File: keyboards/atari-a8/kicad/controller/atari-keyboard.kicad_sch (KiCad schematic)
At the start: 31 parts, among them J101 PLAYER 1, J102 5V, J103 I2C DISPLAY, SW101 RESET, U101 Elite-C, U102 MAX7219, U103 MAX7219, U104 7402, U105 74LS08

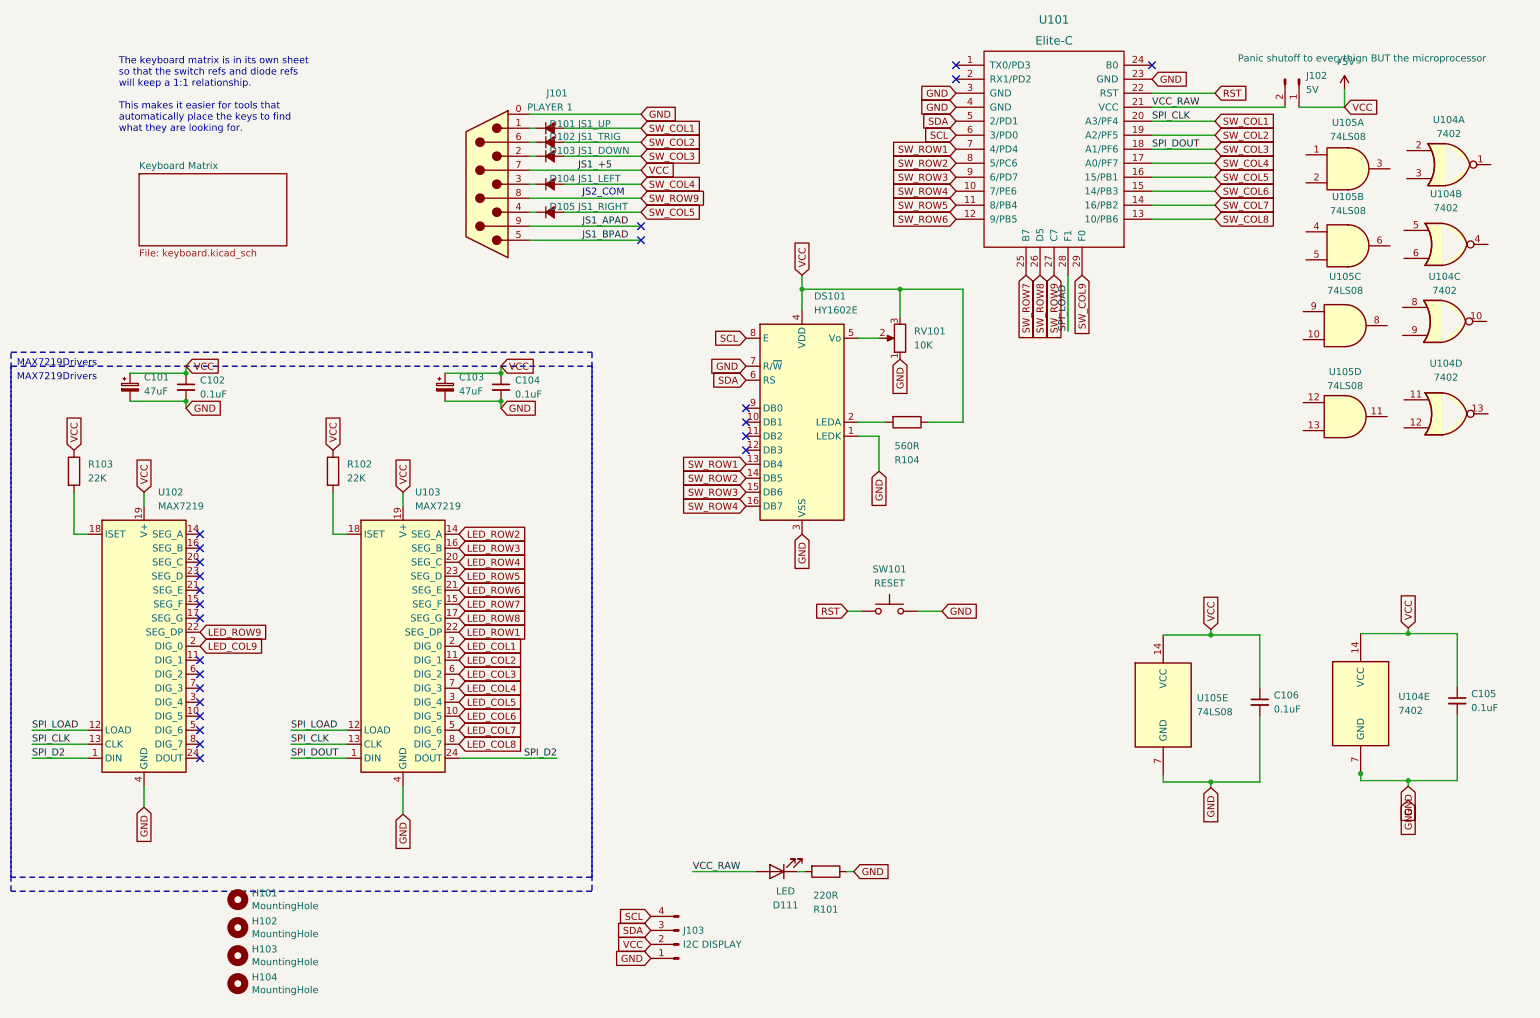
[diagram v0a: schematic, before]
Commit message: Added generating the keyboard plate
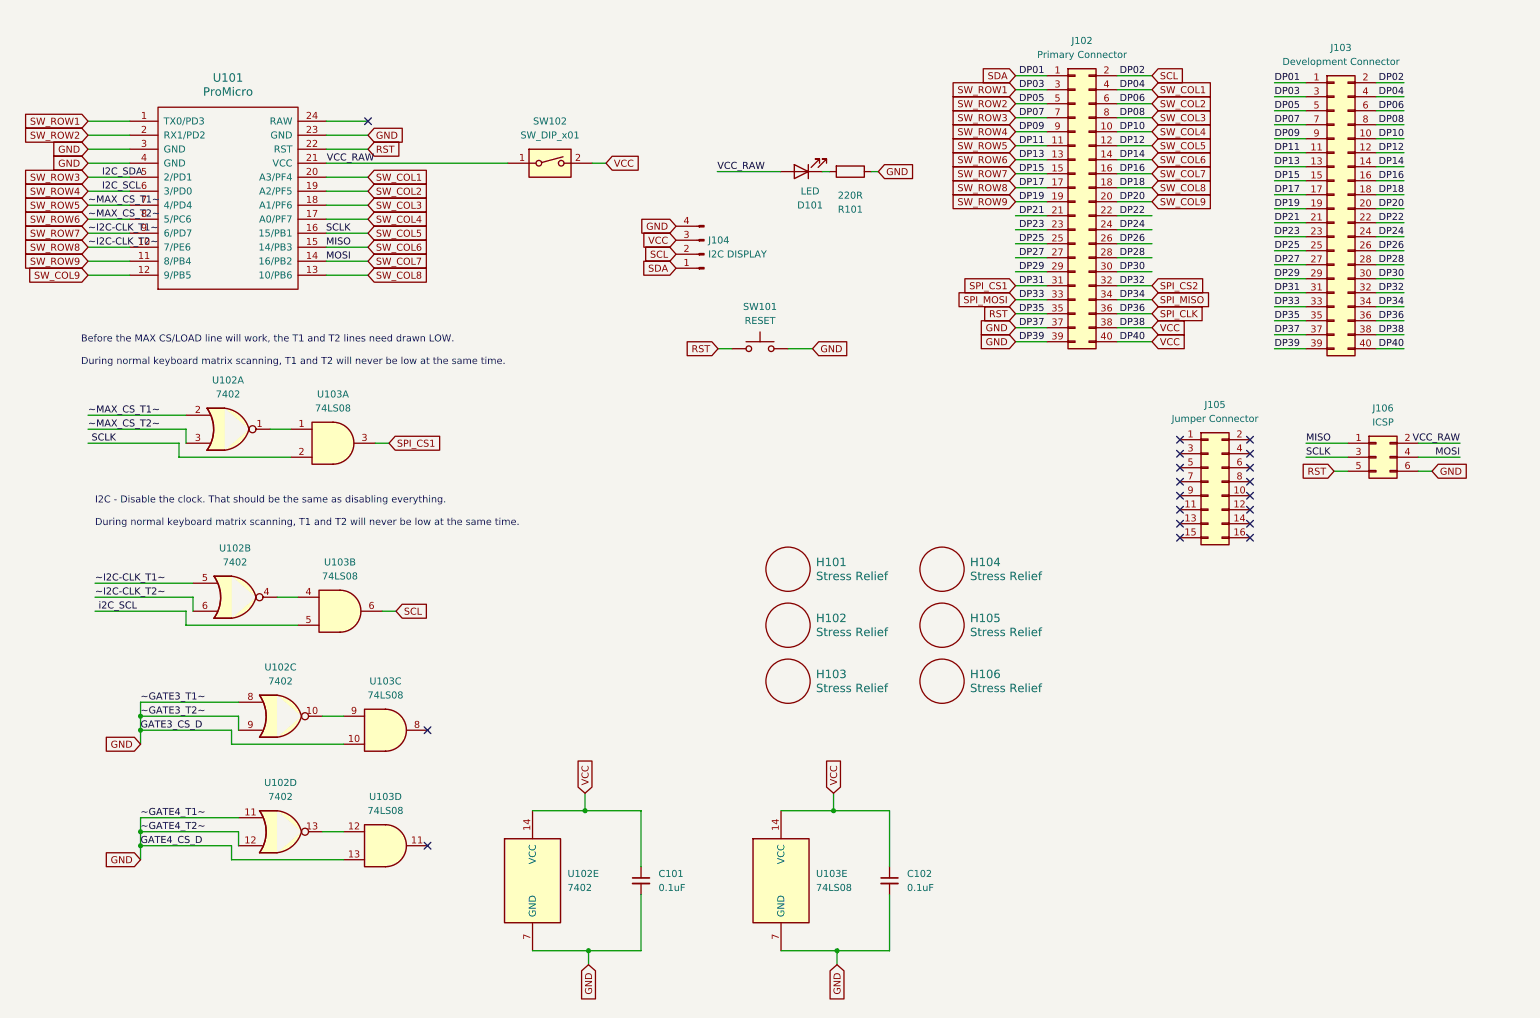
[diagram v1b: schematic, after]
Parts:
- removed C101, C103: 47uF, Capacitor_THT:CP_Radial_D5.0mm_P2.50mm, symbol Device:C_Polarized_Small
- removed C104, C105, C106: 0.1uF, Capacitor_THT:C_Axial_L3.8mm_D2.6mm_P10.00mm_Horizontal, symbol Device:C_Small
- removed D101: JS1_UP, retro-kbd:Diode-dual, symbol atari-keyboard-rescue:D_Small_ALT-Device
- removed D102: JS1_TRIG, retro-kbd:Diode-dual, symbol atari-keyboard-rescue:D_Small_ALT-Device
- removed D103: JS1_DOWN, retro-kbd:Diode-dual, symbol atari-keyboard-rescue:D_Small_ALT-Device
- removed D104: JS1_LEFT, retro-kbd:Diode-dual, symbol atari-keyboard-rescue:D_Small_ALT-Device
- removed D105: JS1_RIGHT, retro-kbd:Diode-dual, symbol atari-keyboard-rescue:D_Small_ALT-Device
- removed DS101: HY1602E, Display:HY1602E, symbol Display_Character:HY1602E
- removed H101, H102, H103, H104: MountingHole, MountingHole:MountingHole_3.2mm_M3, symbol Mechanical:MountingHole
- removed J101: PLAYER 1, Connector_Dsub:DSUB-9_Male_Horizontal_P2.77x2.84mm_EdgePinOffset9.90mm_Housed_MountingHolesOffset11.32mm, symbol jsconnector:DB9_Male
- removed J102: 5V, Connector_PinHeader_2.54mm:PinHeader_1x02_P2.54mm_Vertical, symbol Connector:Conn_01x02_Pin
- removed R102, R103: 22K, keebio:Resistor-Hybrid, symbol Device:R
- removed R104: 560R, keebio:Resistor-Hybrid, symbol Device:R
- removed RV101: 10K, Potentiometer_THT:Potentiometer_ACP_CA9-V10_Vertical, symbol Device:R_Potentiometer
- removed U101: Elite-C, keebio:Elite-C-castellated-29pin-holes, symbol keebio:Elite-C
- removed U102, U103: MAX7219, Package_DIP:DIP-24_W7.62mm_Socket_LongPads, symbol Driver_LED:MAX7219
- removed U104: 7402, Package_DIP:DIP-14_W7.62mm_Socket_LongPads, symbol 74xx:7402
- removed U105: 74LS08, Package_DIP:DIP-14_W7.62mm_Socket_LongPads, symbol 74xx:74LS08
- added C101: 0.1uF, Capacitor_THT:C_Axial_L3.8mm_D2.6mm_P7.50mm_Horizontal, symbol Device:C_Small
- added H101, H102, H103, H104, H105, H106: Stress Relief, MountingHole:MountingHole_2.7mm, symbol keebio:Hole
- added J102: Primary Connector, Connector_PinHeader_2.54mm:PinHeader_2x20_P2.54mm_Vertical, symbol Connector_Generic:Conn_02x20_Odd_Even
- added J103: Development Connector, Connector_PinHeader_2.54mm:PinHeader_2x20_P2.54mm_Vertical, symbol Connector_Generic:Conn_02x20_Odd_Even
- added J105: Jumper Connector, Connector_PinHeader_2.54mm:PinHeader_2x08_P2.54mm_Vertical, symbol Connector_Generic:Conn_02x08_Odd_Even
- added J106: ICSP, Connector_PinHeader_2.54mm:PinHeader_2x03_P2.54mm_Vertical, symbol Connector_Generic:Conn_02x03_Odd_Even
- added SW102: SW_DIP_x01, Button_Switch_THT:SW_DIP_SPSTx01_Slide_9.78x4.72mm_W7.62mm_P2.54mm, symbol Switch:SW_DIP_x01
- added U101: ProMicro, promicro:ProMicro, symbol keebio:ProMicro
- added U102: 7402, Package_DIP:DIP-14_W7.62mm_Socket, symbol 74xx:7402
- added U103: 74LS08, Package_DIP:DIP-14_W7.62mm_Socket, symbol 74xx:74LS08
- C102: footprint Capacitor_THT:C_Axial_L3.8mm_D2.6mm_P10.00mm_Horizontal -> Capacitor_THT:C_Axial_L3.8mm_D2.6mm_P7.50mm_Horizontal
- renumbered D111 to D101, J103 to J104
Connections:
- net GND: now also J104.4 (Pin_4), C101.2, J102.37 (Pin_37), J102.39 (Pin_39), J103.37 (Pin_37), J103.39 (Pin_39), J106.6 (Pin_6), U101.23 (GND), U101.3 (GND), U101.4 (GND), U102.11, U102.12, U102.7 (GND), U102.8, U102.9, U103.10, U103.13, U103.7 (GND); no longer J104.1 (Pin_1)
- net RST: now also J102.35 (Pin_35), J103.35 (Pin_35), J106.5 (Pin_5), U101.22 (RST)
- net SCL: now also J104.2 (Pin_2), J102.2 (Pin_2), J103.2 (Pin_2), U103.6; no longer J104.4 (Pin_4)
- net SDA: now also J104.1 (Pin_1), J102.1 (Pin_1), J103.1 (Pin_1); no longer J104.3 (Pin_3)
- net SW_COL1: now also J102.4 (Pin_4), J103.4 (Pin_4), U101.20 (A3/PF4)
- net SW_COL2: now also J102.6 (Pin_6), J103.6 (Pin_6), U101.19 (A2/PF5)
- net SW_COL3: now also J102.8 (Pin_8), J103.8 (Pin_8), U101.18 (A1/PF6)
- net SW_COL4: now also J102.10 (Pin_10), J103.10 (Pin_10), U101.17 (A0/PF7)
- net SW_COL5: now also J102.12 (Pin_12), J103.12 (Pin_12), J106.3 (Pin_3), U101.16 (15/PB1), U103.2
- net SW_COL6: now also J102.14 (Pin_14), J103.14 (Pin_14), J106.1 (Pin_1), U101.15 (14/PB3)
- net SW_COL7: now also J102.16 (Pin_16), J103.16 (Pin_16), J106.4 (Pin_4), U101.14 (16/PB2)
- net SW_COL8: now also J102.18 (Pin_18), J103.18 (Pin_18), U101.13 (10/PB6)
- net SW_COL9: now also J102.20 (Pin_20), J103.20 (Pin_20), U101.12 (9/PB5)
- net SW_ROW1: now also J102.3 (Pin_3), J103.3 (Pin_3), U101.1 (TX0/PD3)
- net SW_ROW2: now also J102.5 (Pin_5), J103.5 (Pin_5), U101.2 (RX1/PD2)
- net SW_ROW3: now also J102.7 (Pin_7), J103.7 (Pin_7), U101.5 (2/PD1)
- net SW_ROW4: now also J102.9 (Pin_9), J103.9 (Pin_9), U101.6 (3/PD0)
- net SW_ROW5: now also J102.11 (Pin_11), J103.11 (Pin_11), U101.7 (4/PD4), U102.2
- net SW_ROW6: now also J102.13 (Pin_13), J103.13 (Pin_13), U101.8 (5/PC6), U102.3
- net SW_ROW7: now also J102.15 (Pin_15), J103.15 (Pin_15), U101.9 (6/PD7), U102.5
- net SW_ROW8: now also J102.17 (Pin_17), J103.17 (Pin_17), U101.10 (7/PE6), U102.6
- net SW_ROW9: now also J102.19 (Pin_19), J103.19 (Pin_19), U101.11 (8/PB4)
- net VCC_RAW: now also J106.2 (Pin_2), SW102.1, U101.21 (VCC)
- net +5V renamed VCC
- net VCC: now also J104.3 (Pin_3), C101.1, J102.38 (Pin_38), J102.40 (Pin_40), J103.38 (Pin_38), J103.40 (Pin_40), SW102.2, U102.14 (VCC), U103.14 (VCC); no longer J104.2 (Pin_2)
- new net: U102.10, U103.9
- new net: U102.1, U103.1
- new net: U102.13, U103.12
- new net: U102.4, U103.4
- new net DP21: J102.21 (Pin_21), J103.21 (Pin_21)
- new net DP22: J102.22 (Pin_22), J103.22 (Pin_22)
- new net DP23: J102.23 (Pin_23), J103.23 (Pin_23)
- new net DP24: J102.24 (Pin_24), J103.24 (Pin_24)
- new net DP25: J102.25 (Pin_25), J103.25 (Pin_25)
- new net DP26: J102.26 (Pin_26), J103.26 (Pin_26)
- new net DP27: J102.27 (Pin_27), J103.27 (Pin_27)
- new net DP28: J102.28 (Pin_28), J103.28 (Pin_28)
- new net DP29: J102.29 (Pin_29), J103.29 (Pin_29)
- new net DP30: J102.30 (Pin_30), J103.30 (Pin_30)
- new net SPI_CLK: J102.36 (Pin_36), J103.36 (Pin_36)
- new net SPI_CS1: J102.31 (Pin_31), J103.31 (Pin_31), U103.3
- new net SPI_CS2: J102.32 (Pin_32), J103.32 (Pin_32)
- new net SPI_MISO: J102.34 (Pin_34), J103.34 (Pin_34)
- new net SPI_MOSI: J102.33 (Pin_33), J103.33 (Pin_33)
- new net i2C_SCL: U103.5
- no-connect marks 24 -> 19
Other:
- removed sheet Keyboard Matrix
- note added: "Before the MAX CS/LOAD line will work, the T1 and T2 lines need drawn LOW. During normal keyboard matrix scanning, T1 and T2 will never be low at the same time."
- note added: "I2C - Disable the clock. That should be the same as disabling everything. During normal keyboard matrix scanning, T1 and T2 will never be low at the same time."
- note removed: "JS2_COM"
- note removed: "The keyboard matrix is in its own sheet so that the switch refs and diode refs will keep a 1:1 relationship. This makes it easier for tools that automatically place the keys to find what they are looking for."
- moved on the sheet: D101, J104, R101, SW101
